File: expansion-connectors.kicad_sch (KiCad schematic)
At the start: 6 parts, among them J10 LSHM-130-01-L-RH-A-S-K-TR

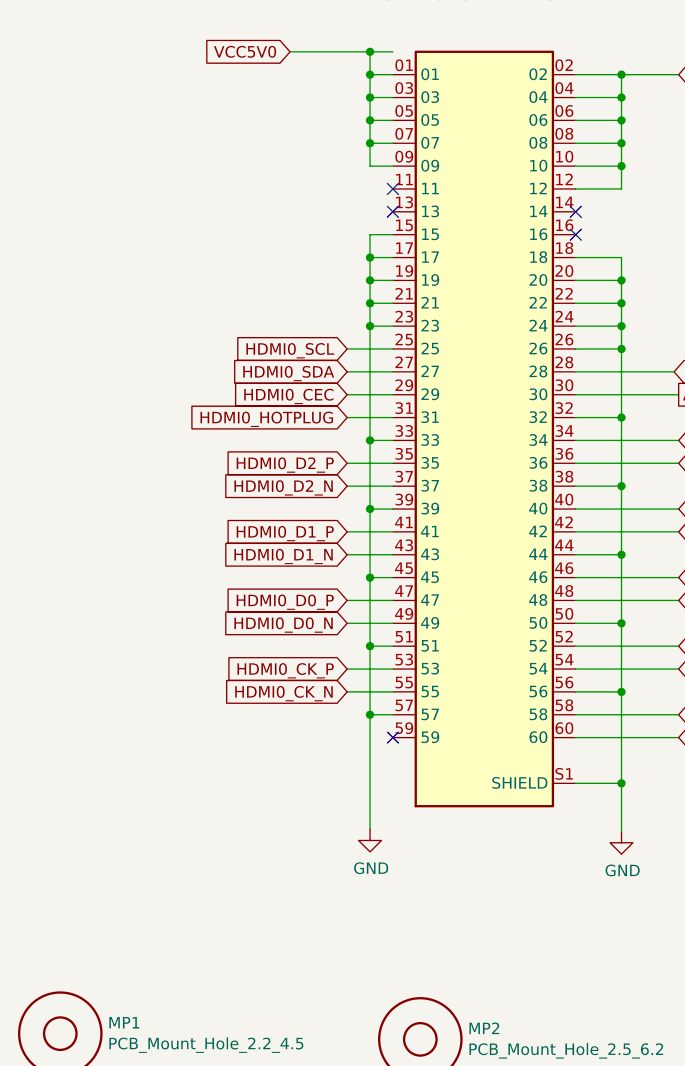
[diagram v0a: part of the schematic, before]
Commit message: Updated badly connected J10
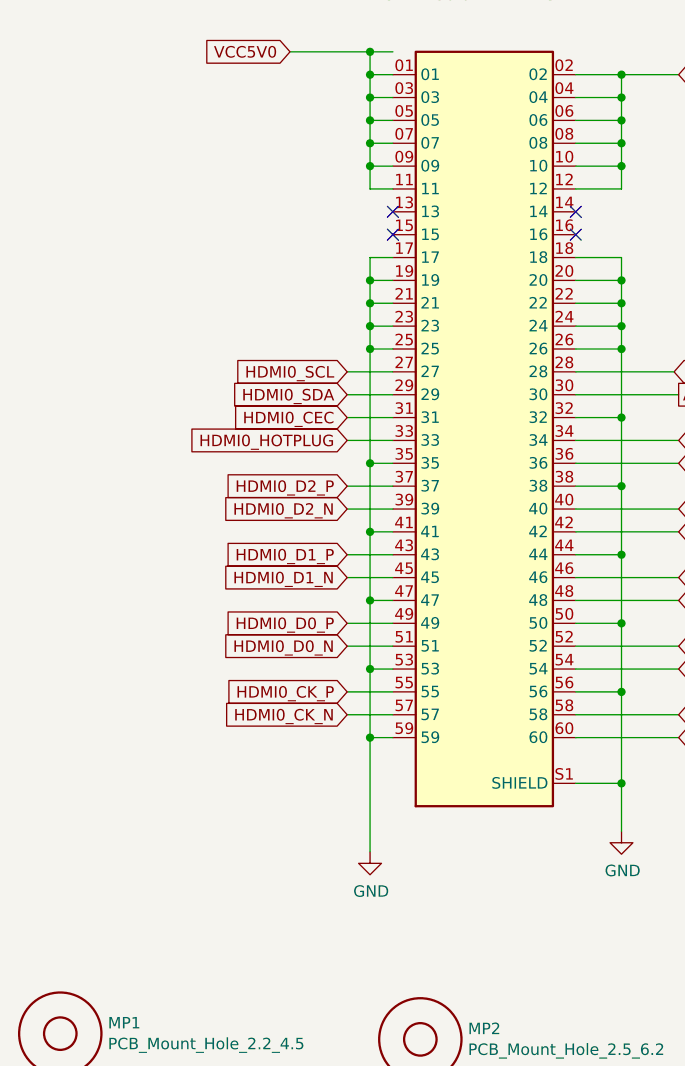
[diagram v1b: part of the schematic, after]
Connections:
- net GND: now also J10.25, J10.35, J10.41, J10.47, J10.53, J10.59; no longer J10.15, J10.33, J10.39, J10.45, J10.51, J10.57
- net HDMI0_CEC: now also J10.31; no longer J10.29
- net HDMI0_CK_N: now also J10.57; no longer J10.55
- net HDMI0_CK_P: now also J10.55; no longer J10.53
- net HDMI0_D0_N: now also J10.51; no longer J10.49
- net HDMI0_D0_P: now also J10.49; no longer J10.47
- net HDMI0_D1_N: now also J10.45; no longer J10.43
- net HDMI0_D1_P: now also J10.43; no longer J10.41
- net HDMI0_D2_N: now also J10.39; no longer J10.37
- net HDMI0_D2_P: now also J10.37; no longer J10.35
- net HDMI0_HOTPLUG: now also J10.33; no longer J10.31
- net HDMI0_SCL: now also J10.27; no longer J10.25
- net HDMI0_SDA: now also J10.29; no longer J10.27
- net VCC5V0: now also J10.11
- no-connect marks 5 -> 4

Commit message: [#46875] WIP project update
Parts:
- J10: MANUFACTURER Samtec -> (none); MAXIMUM_PACKAGE_HEIGHT 5.13 mm -> (none)
- MP1, MP2, MP3: Manufacturer None -> (none)
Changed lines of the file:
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@@
   )
   (text "LSHM connector current rating:\n2A per pin (2 pins powered)"
-    (at 245.11 82.55 180)
+    (at 245.11 82.55 0)
     (effects (font (size 1.27 1.27)) (justify right bottom))
   )
@@
   (symbol (lib_id "antmicroMechanicalParts:PCB_Mount_Hole_2.2_4.5") (at 135.255 196.215 0) (unit 1)
     (in_bom yes) (on_board yes)
-    (property "Reference" "MP1" (id 0) (at 140.5382 195.0466 0)
-      (effects (font (size 1.27 1.27)) (justify left))
-    )
-    (property "Value" "PCB_Mount_Hole_2.2_4.5" (id 1) (at 140.5382 197.358 0)
-      (effects (font (size 1.27 1.27)) (justify left))
+    (property "Reference" "MP1" (id 0) (at 153.035 198.755 0)
+      (effects (font (size 1.27 1.27) (thickness 0.15)) (justify left bottom))
+    )
+    (property "Value" "PCB_Mount_Hole_2.2_4.5" (id 1) (at 153.035 201.295 0)
+      (effects (font (size 1.27 1.27) (thickness 0.15)) (justify left bottom))
     )
     (property "Footprint" "antmicro-footprints:mounting-hole-2.2mm" (id 2) (at 153.035 203.835 0)
@@
       (effects (font (size 1.27 1.27) (thickness 0.15)) (justify left bottom) hide)
     )
-    (property "Manufacturer" "None" (id 4) (at 153.035 206.375 0)
+    (property "Manufacturer" "" (id 4) (at 153.035 206.375 0)
       (effects (font (size 1.27 1.27) (thickness 0.15)) (justify left bottom) hide)
     )
@@
       (effects (font (size 1.27 1.27) (thickness 0.15)) (justify left bottom) hide)
     )
+    (property "MPN" "" (id 7) (at 135.255 196.215 0)
+      (effects (font (size 1.27 1.27)) hide)
+    )
   )
   (symbol (lib_id "antmicroMechanicalParts:PCB_Mount_Hole_2.5_6.2") (at 175.26 196.85 0) (unit 1)
     (in_bom yes) (on_board yes)
-    (property "Reference" "MP2" (id 0) (at 180.5432 195.6816 0)
-      (effects (font (size 1.27 1.27)) (justify left))
-    )
-    (property "Value" "PCB_Mount_Hole_2.5_6.2" (id 1) (at 180.5432 197.993 0)
-      (effects (font (size 1.27 1.27)) (justify left))
+    (property "Reference" "MP2" (id 0) (at 193.04 199.39 0)
+      (effects (font (size 1.27 1.27) (thickness 0.15)) (justify left bottom))
+    )
+    (property "Value" "PCB_Mount_Hole_2.5_6.2" (id 1) (at 193.04 201.93 0)
+      (effects (font (size 1.27 1.27) (thickness 0.15)) (justify left bottom))
     )
     (property "Footprint" "antmicro-footprints:Mount-hole-M2.5" (id 2) (at 193.04 204.47 0)
@@
       (effects (font (size 1.27 1.27) (thickness 0.15)) (justify left bottom) hide)
     )
-    (property "Manufacturer" "None" (id 4) (at 193.04 209.55 0)
+    (property "Manufacturer" "" (id 4) (at 193.04 209.55 0)
       (effects (font (size 1.27 1.27) (thickness 0.15)) (justify left bottom) hide)
     )
@@
       (effects (font (size 1.27 1.27) (thickness 0.15)) (justify left bottom) hide)
     )
+    (property "MPN" "" (id 7) (at 175.26 196.85 0)
+      (effects (font (size 1.27 1.27)) hide)
+    )
   )
   (symbol (lib_id "antmicroMechanicalParts:PCB_Mount_Hole_2.5_6.2") (at 213.36 196.85 0) (unit 1)
     (in_bom yes) (on_board yes)
-    (property "Reference" "MP3" (id 0) (at 218.6432 195.6816 0)
-      (effects (font (size 1.27 1.27)) (justify left))
-    )
-    (property "Value" "PCB_Mount_Hole_2.5_6.2" (id 1) (at 218.6432 197.993 0)
-      (effects (font (size 1.27 1.27)) (justify left))
+    (property "Reference" "MP3" (id 0) (at 231.14 199.39 0)
+      (effects (font (size 1.27 1.27) (thickness 0.15)) (justify left bottom))
+    )
+    (property "Value" "PCB_Mount_Hole_2.5_6.2" (id 1) (at 231.14 201.93 0)
+      (effects (font (size 1.27 1.27) (thickness 0.15)) (justify left bottom))
     )
     (property "Footprint" "antmicro-footprints:Mount-hole-M2.5" (id 2) (at 231.14 204.47 0)
@@
       (effects (font (size 1.27 1.27) (thickness 0.15)) (justify left bottom) hide)
     )
-    (property "Manufacturer" "None" (id 4) (at 231.14 209.55 0)
+    (property "Manufacturer" "" (id 4) (at 231.14 209.55 0)
       (effects (font (size 1.27 1.27) (thickness 0.15)) (justify left bottom) hide)
     )
@@
       (effects (font (size 1.27 1.27) (thickness 0.15)) (justify left bottom) hide)
     )
+    (property "MPN" "" (id 7) (at 213.36 196.85 0)
+      (effects (font (size 1.27 1.27)) hide)
+    )
   )
   (symbol (lib_id "antmicroB2bConnectors:LSHM-130-01-L-RH-A-S-K-TR") (at 172.212 89.662 0) (unit 1)
     (in_bom yes) (on_board yes)
-    (property "Reference" "J10" (id 0) (at 182.626 77.724 0))
-    (property "Value" "LSHM-130-01-L-RH-A-S-K-TR" (id 1) (at 182.626 80.772 0))
+    (property "Reference" "J10" (id 0) (at 207.772 92.202 0)
+      (effects (font (size 1.27 1.27) (thickness 0.15)) (justify left bottom))
+    )
+    (property "Value" "LSHM-130-01-L-RH-A-S-K-TR" (id 1) (at 207.772 94.742 0)
+      (effects (font (size 1.27 1.27) (thickness 0.15)) (justify left bottom))
+    )
     (property "Footprint" "antmicro-footprints:SAMTEC_LSHM-130-01-XXX-RH-A-S-K-XX" (id 2) (at 207.772 97.282 0)
       (effects (font (size 1.27 1.27) (thickness 0.15)) (justify left bottom) hide)
@@
       (effects (font (size 1.27 1.27) (thickness 0.15)) (justify left bottom) hide)
     )
-    (property "MANUFACTURER" "Samtec" (id 4) (at 172.212 89.662 0)
-      (effects (font (size 1.27 1.27)) (justify left bottom) hide)
-    )
     (property "MPN" "LSHM-130-01-L-RH-A-S-K-TR" (id 5) (at 207.772 104.902 0)
       (effects (font (size 1.27 1.27) (thickness 0.15)) (justify left bottom) hide)
-    )
-    (property "MAXIMUM_PACKAGE_HEIGHT" "5.13 mm" (id 6) (at 172.212 89.662 0)
-      (effects (font (size 1.27 1.27)) (justify left bottom) hide)
     )
     (property "Manufacturer" "Samtec" (id 7) (at 207.772 102.362 0)
@@
   (symbol (lib_id "antmicroResistorsmisc:R_0R_1206") (at 264.16 99.06 0) (unit 1)
     (in_bom yes) (on_board yes)
-    (property "Reference" "R62" (id 0) (at 264.668 97.028 0)
-      (effects (font (size 1.524 1.524)))
-    )
-    (property "Value" "R_0R_1206" (id 1) (at 264.16 102.87 0)
-      (effects (font (size 1.524 1.524)) hide)
+    (property "Reference" "R62" (id 0) (at 284.48 104.14 0)
+      (effects (font (size 1.27 1.27) (thickness 0.15)) (justify left bottom))
+    )
+    (property "Value" "R_0R_1206" (id 1) (at 284.48 111.76 0)
+      (effects (font (size 1.27 1.27) (thickness 0.15)) (justify left bottom) hide)
     )
     (property "Footprint" "antmicro-footprints:R_1206_3216Metric" (id 2) (at 284.48 114.3 0)
@@
       (effects (font (size 1.27 1.27) (thickness 0.15)) (justify left bottom) hide)
     )
-    (property "Val" "0R" (id 6) (at 267.716 98.044 0)
+    (property "Val" "0R" (id 6) (at 284.48 106.68 0)
       (effects (font (size 1.27 1.27) (thickness 0.15)) (justify left bottom))
     )
@@
       (effects (font (size 1.27 1.27)) (justify left bottom) hide)
     )
-    (property "Current" "2A" (id 10) (at 271.018 98.044 0)
-      (effects (font (size 1.27 1.27) (thickness 0.15)) (justify left bottom))
+    (property "Current" "2A" (id 10) (at 284.48 129.54 0)
+      (effects (font (size 1.27 1.27) (thickness 0.15)) (justify left bottom) hide)
     )
     (pin "1")
@@
       (effects (font (size 1.27 1.27)) hide)
     )
-    (property "Value" "GND" (id 1) (at 197.739 178.1302 0))
+    (property "Value" "GND" (id 1) (at 197.612 177.546 0))
     (property "Footprint" "" (id 2) (at 197.612 173.736 0)
       (effects (font (size 1.27 1.27)) hide)
@@
   (symbol (lib_id "antmicroResistorsmisc:R_0R_1206") (at 264.16 103.632 0) (unit 1)
     (in_bom yes) (on_board yes)
-    (property "Reference" "R63" (id 0) (at 264.922 101.6 0)
-      (effects (font (size 1.524 1.524)))
-    )
-    (property "Value" "R_0R_1206" (id 1) (at 264.16 107.442 0)
-      (effects (font (size 1.524 1.524)) hide)
+    (property "Reference" "R63" (id 0) (at 284.48 108.712 0)
+      (effects (font (size 1.27 1.27) (thickness 0.15)) (justify left bottom))
+    )
+    (property "Value" "R_0R_1206" (id 1) (at 284.48 116.332 0)
+      (effects (font (size 1.27 1.27) (thickness 0.15)) (justify left bottom) hide)
     )
     (property "Footprint" "antmicro-footprints:R_1206_3216Metric" (id 2) (at 284.48 118.872 0)
@@
       (effects (font (size 1.27 1.27) (thickness 0.15)) (justify left bottom) hide)
     )
-    (property "Val" "0R" (id 6) (at 267.716 102.616 0)
+    (property "Val" "0R" (id 6) (at 284.48 111.252 0)
       (effects (font (size 1.27 1.27) (thickness 0.15)) (justify left bottom))
     )
@@
       (effects (font (size 1.27 1.27)) (justify left bottom) hide)
     )
-    (property "Current" "2A" (id 11) (at 271.272 102.616 0)
-      (effects (font (size 1.27 1.27) (thickness 0.15)) (justify left bottom))
+    (property "Current" "2A" (id 11) (at 284.48 134.112 0)
+      (effects (font (size 1.27 1.27) (thickness 0.15)) (justify left bottom) hide)
     )
     (pin "1")
@@
       (effects (font (size 1.27 1.27)) hide)
     )
-    (property "Value" "GND" (id 1) (at 169.799 180.4162 0))
+    (property "Value" "GND" (id 1) (at 169.672 179.832 0))
     (property "Footprint" "" (id 2) (at 169.672 176.022 0)
       (effects (font (size 1.27 1.27)) hide)

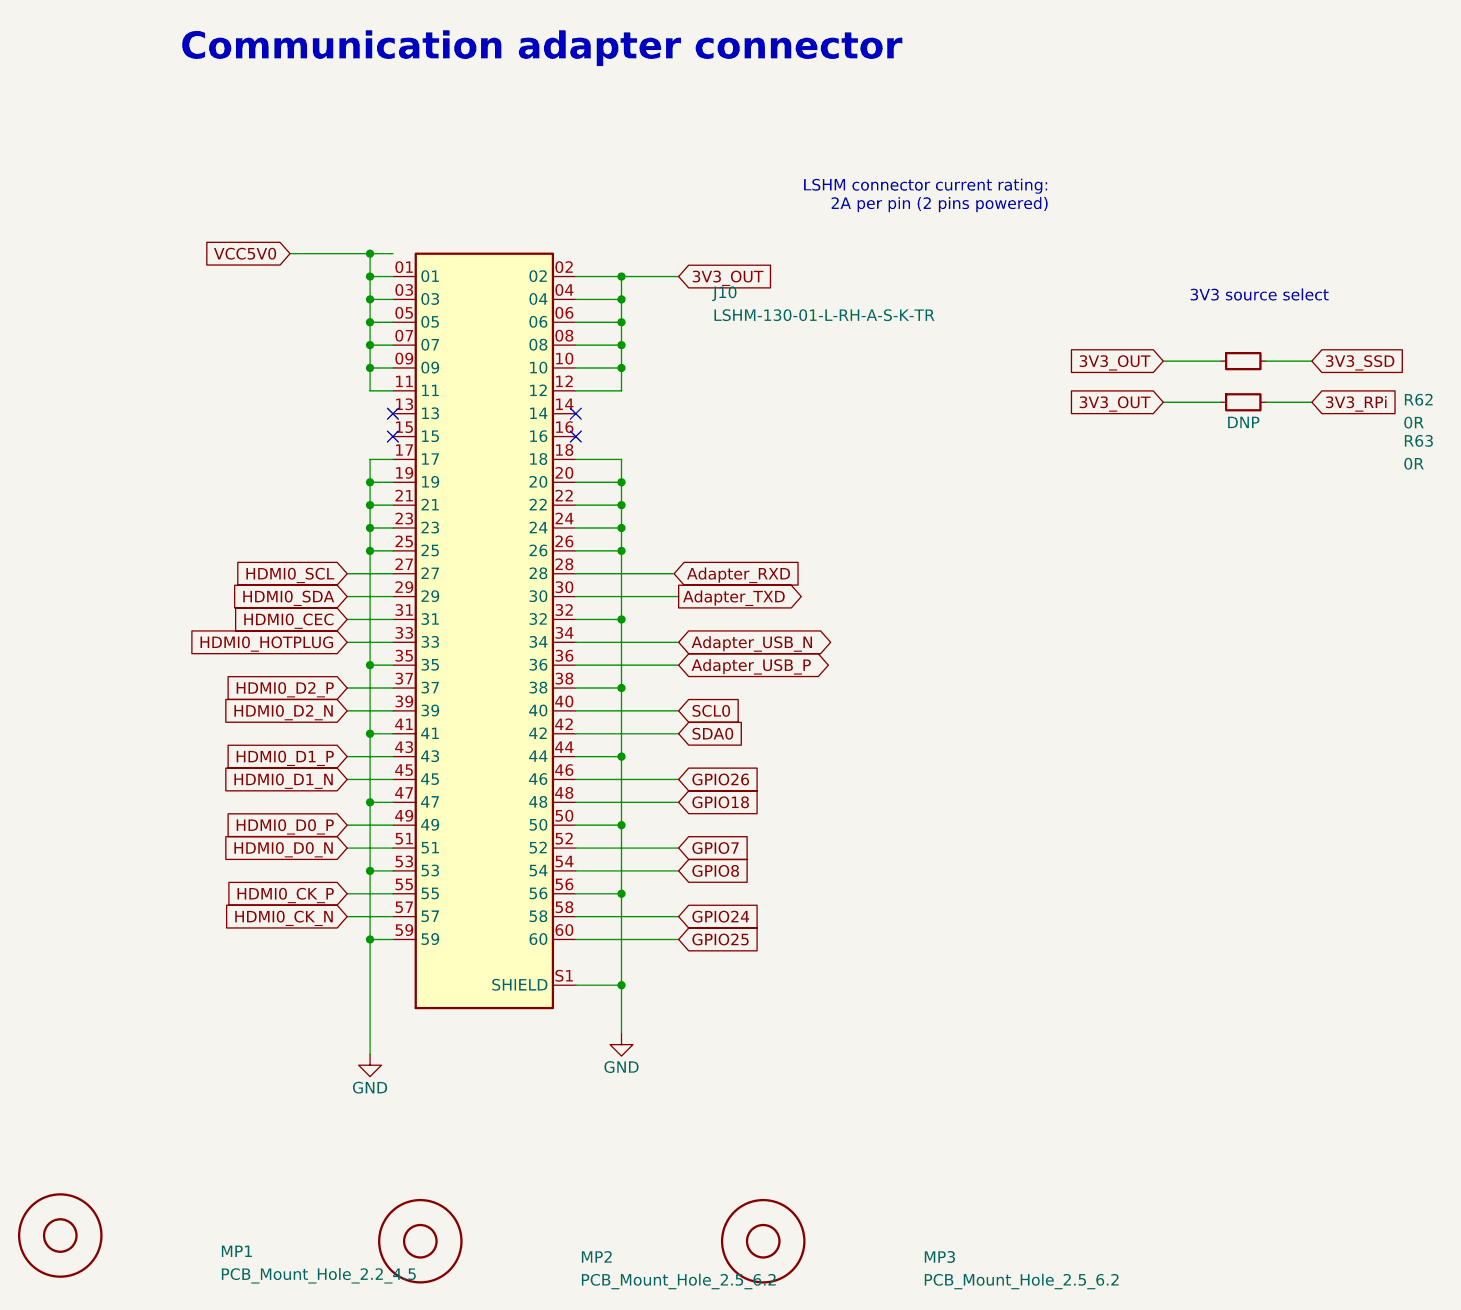
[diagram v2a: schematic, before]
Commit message: [#46875] Standardize schematics
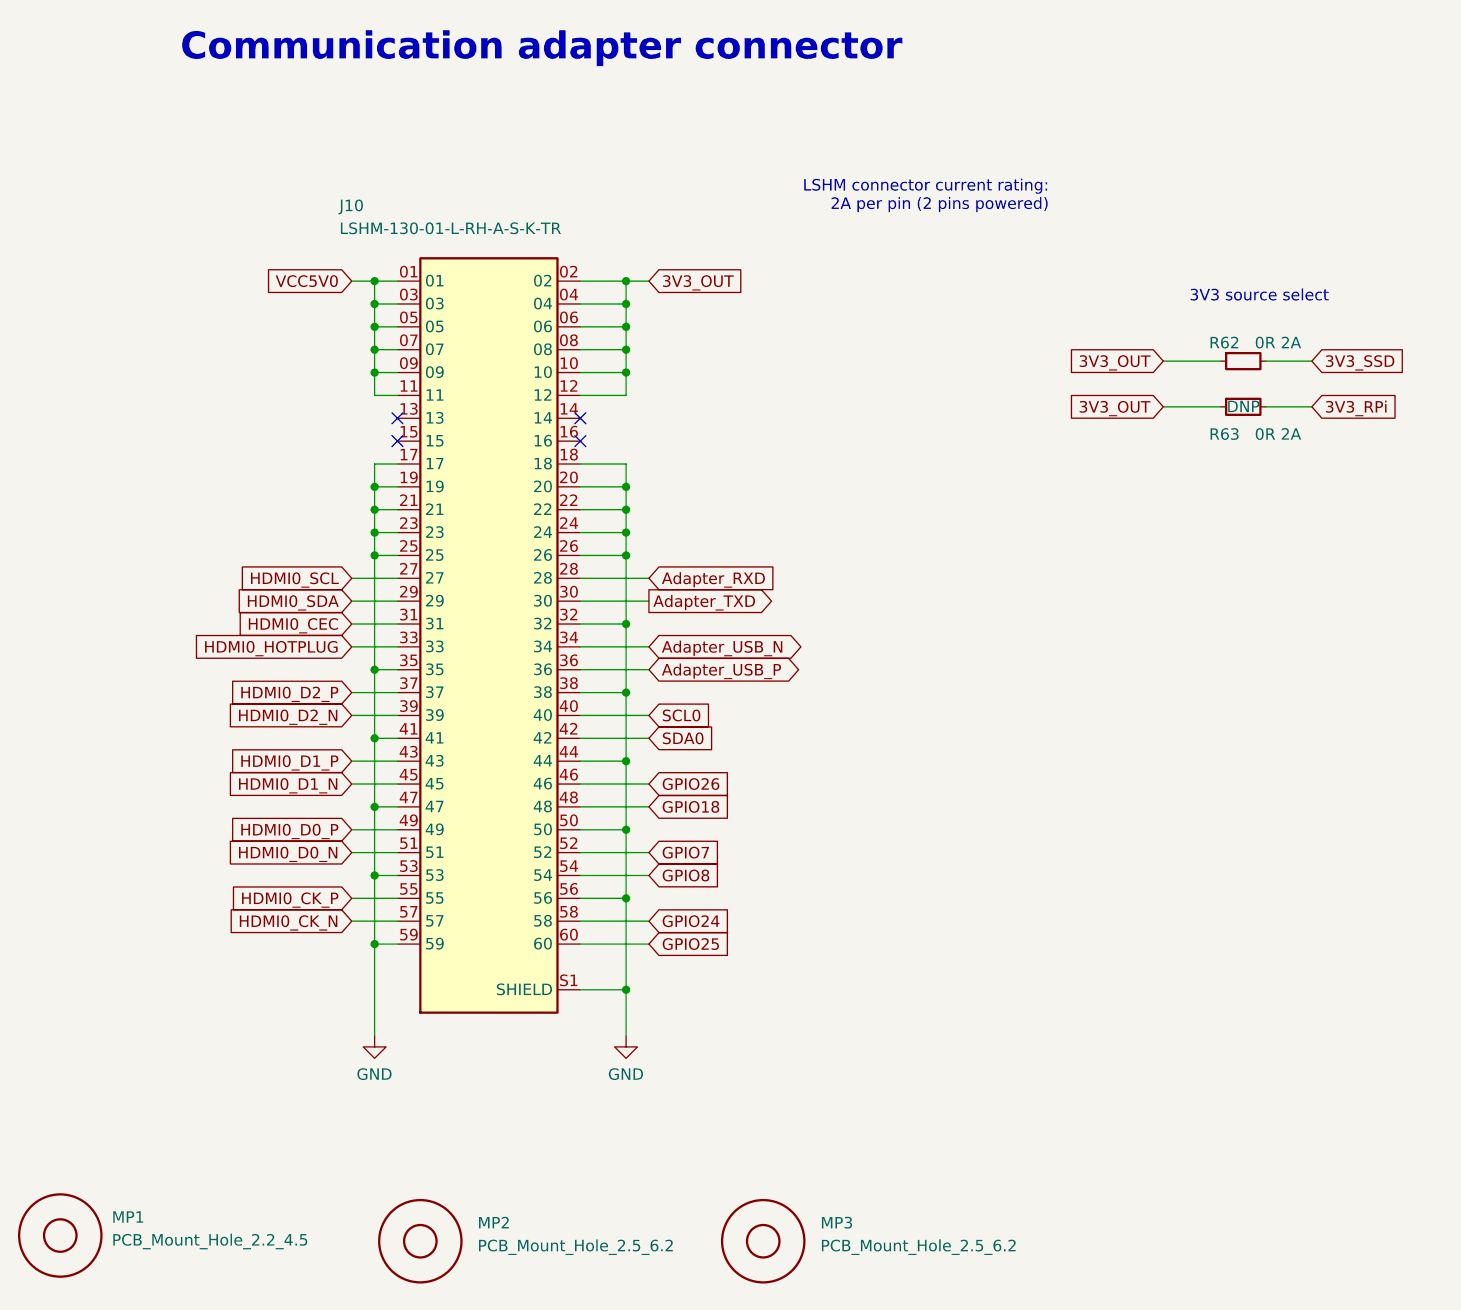
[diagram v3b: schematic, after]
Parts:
- R62, R63: Val 0R -> 0R 2A
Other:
- moved on the sheet: J10, R63
